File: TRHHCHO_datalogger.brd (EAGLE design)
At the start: 49.1 x 50.8 mm, 39 parts, among them J6 AMP FCI 10103594-0001LF, U1 ATMEGA328P-MU, U10 TSL2591, U2 FT231XQ-R, U3 DS3234, U7 SHT31/35, U8 MCP1703/3.3V, Y2 SPARKFUN_RESONATORSMD

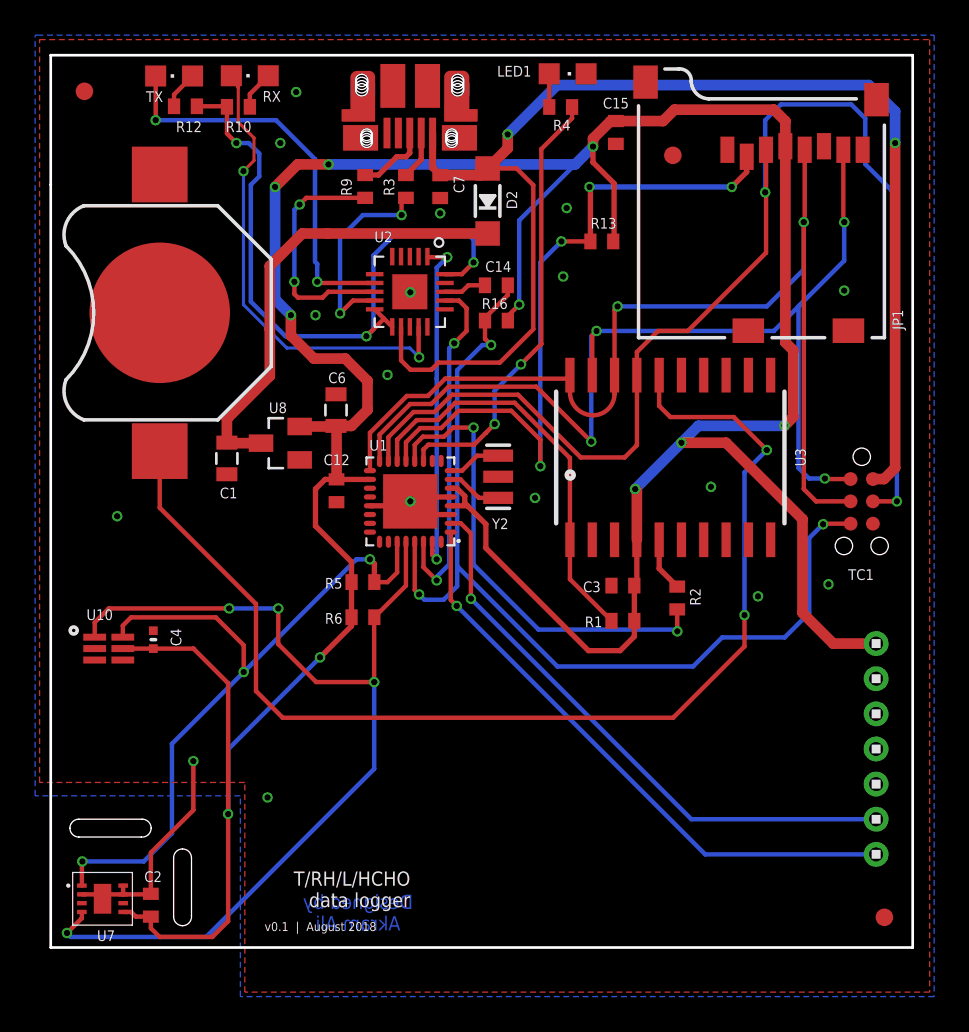
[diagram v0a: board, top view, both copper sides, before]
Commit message: Updated footprint of HCHO sensor
- Now using proper dimensions given by manufacturer
- Small trace adjustments
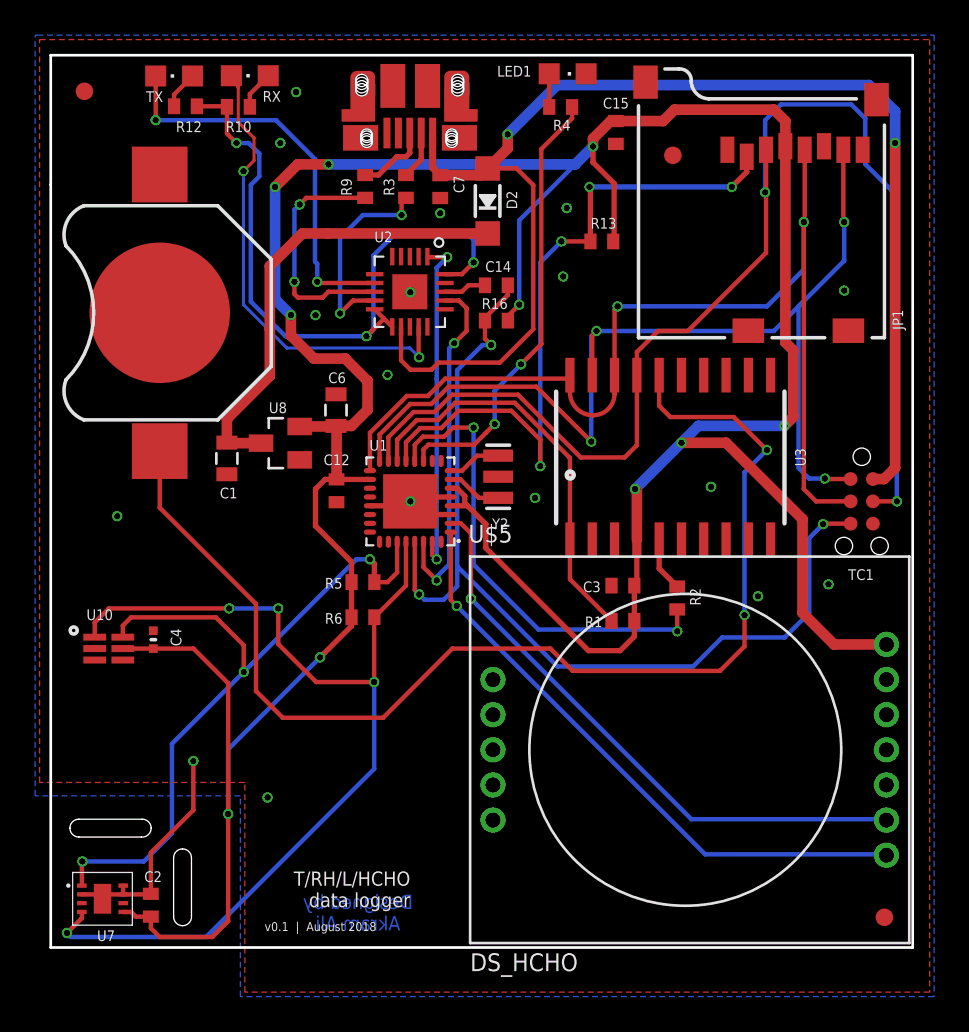
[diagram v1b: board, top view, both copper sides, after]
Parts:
- removed U$4: 1X7, headers(2mm):1X7
- added U$5: DS_HCHO, Plantower-DS-HCHO:DS_HCHO
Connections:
- net D3: now also U$5.P$7; no longer U$4.1
- net D4: now also U$5.P$6; no longer U$4.2
- net GND: now also U$5.P$2; no longer U$4.6
- net VCC: now also U$5.P$1; no longer U$4.7
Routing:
- net N$8: track 66.7 -> 67.7 mm
- net D4: track 33.4 -> 34.0 mm
- net D3: track 34.1 -> 34.7 mm
- net VCC: track 197.5 -> 198.1 mm
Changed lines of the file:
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@@
 <attribute name="NAME" x="33.5382" y="49.5832" size="0.6096" layer="25" font="vector"/>
 </element>
-<element name="U8" library="linear" library_urn="urn:adsk.eagle:library:262" package="SOT23" value="MCP1703/3.3V" x="21.1992" y="28.7124" smashed="yes" rot="R90">
+<element name="U8" library="linear" library_urn="urn:adsk.eagle:library:262" package="SOT23" package3d_urn="urn:adsk.eagle:package:16489/2" value="MCP1703/3.3V" x="21.1992" y="28.7124" smashed="yes" rot="R90">
 <attribute name="MPN" value="MCP1703T-2502E/CB" x="21.1992" y="28.7124" size="1.778" layer="27" rot="R90" display="off"/>
 <attribute name="NAME" x="21.5766" y="31.0322" size="0.6096" layer="25" font="vector" rot="R180"/>
@@
 <attribute name="PROD_ID" value="CONN-13711" x="28.6" y="47.7" size="1.778" layer="27" rot="R180" display="off"/>
 </element>
-<element name="U$4" library="headers(2mm)" package="1X7" value="1X7" x="55.118" y="11.303" rot="R90"/>
 <element name="U10" library="TSL2591" package="DFN6_TAOS" value="TSL2591" x="11.43" y="17.018" smashed="yes">
 <attribute name="MPN" value="TSL25911FN " x="11.43" y="17.018" size="1.778" layer="27" display="off"/>
@@
 <attribute name="NAME" x="14.9543" y="18.161" size="0.6096" layer="25" font="vector" rot="R270"/>
 </element>
+<element name="U$5" library="Plantower-DS-HCHO" package="DS_HCHO" value="DS_HCHO" x="32.004" y="0.254"/>
 </elements>
 <signals>
@@
 <contactref element="TC1" pad="6"/>
 <contactref element="J6" pad="GND"/>
-<contactref element="U$4" pad="6"/>
 <polygon width="0.254" layer="1">
 <vertex x="7.493" y="51.689"/>
@@
 <contactref element="U10" pad="3"/>
 <contactref element="C4" pad="1"/>
+<contactref element="U$5" pad="P$2"/>
 </signal>
 <signal name="VCC">
@@
 <wire x1="23.114" y1="33.528" x2="21.8" y2="34.842" width="0.6096" layer="1"/>
 <wire x1="21.8" y1="34.842" x2="21.8" y2="36" width="0.6096" layer="1"/>
-<contactref element="U$4" pad="7"/>
-<wire x1="55.118" y1="17.303" x2="52.674" y2="17.303" width="0.6096" layer="1"/>
-<wire x1="52.674" y1="17.303" x2="50.927" y2="19.05" width="0.6096" layer="1"/>
 <wire x1="50.927" y1="19.05" x2="50.927" y2="24.384" width="0.6096" layer="1"/>
 <wire x1="46.5755" y1="28.7355" x2="44.0355" y2="28.7355" width="0.6096" layer="1"/>
@@
 <wire x1="25.252" y1="18.308" x2="25.252" y2="18.8032" width="0.3048" layer="1"/>
 <wire x1="16.256" y1="17.018" x2="13.97" y2="17.018" width="0.254" layer="1"/>
+<contactref element="U$5" pad="P$1"/>
+<wire x1="55.704" y1="17.254" x2="52.723" y2="17.254" width="0.6096" layer="1"/>
+<wire x1="52.723" y1="17.254" x2="50.927" y2="19.05" width="0.6096" layer="1"/>
 </signal>
 <signal name="SCL">
@@
 <wire x1="19.812" y1="19.558" x2="19.812" y2="14.605" width="0.254" layer="1"/>
 <wire x1="19.812" y1="14.605" x2="21.336" y2="13.081" width="0.254" layer="1"/>
-<wire x1="43.561" y1="13.081" x2="47.625" y2="17.145" width="0.254" layer="1"/>
 <wire x1="47.625" y1="17.145" x2="47.625" y2="18.923" width="0.254" layer="1"/>
 <via x="47.625" y="18.923" extent="1-16" drill="0.35"/>
 <wire x1="14.3328" y1="25.0372" x2="19.812" y2="19.558" width="0.254" layer="1"/>
-<wire x1="21.336" y1="13.081" x2="43.561" y2="13.081" width="0.254" layer="1"/>
 <wire x1="47.625" y1="27.051" x2="48.895" y2="28.321" width="0.254" layer="16"/>
 <via x="48.895" y="28.321" extent="1-16" drill="0.35"/>
@@
 <wire x1="47.625" y1="18.923" x2="47.625" y2="27.051" width="0.254" layer="16"/>
 <wire x1="47.016" y1="30.2" x2="43.4" y2="30.2" width="0.254" layer="1"/>
+<wire x1="21.336" y1="13.081" x2="27.051" y2="13.081" width="0.254" layer="1"/>
+<wire x1="27.051" y1="13.081" x2="30.988" y2="17.018" width="0.254" layer="1"/>
+<wire x1="30.988" y1="17.018" x2="36.576" y2="17.018" width="0.254" layer="1"/>
+<wire x1="36.576" y1="17.018" x2="37.846" y2="15.748" width="0.254" layer="1"/>
+<wire x1="37.846" y1="15.748" x2="46.228" y2="15.748" width="0.254" layer="1"/>
+<wire x1="46.228" y1="15.748" x2="47.625" y2="17.145" width="0.254" layer="1"/>
 </signal>
 <signal name="SS">
@@
 <signal name="D3">
 <contactref element="U1" pad="1"/>
-<contactref element="U$4" pad="1"/>
 <wire x1="30.9004" y1="23.6488" x2="30.9004" y2="19.7897" width="0.254" layer="1"/>
 <wire x1="30.9004" y1="19.7897" x2="31.242" y2="19.4481" width="0.254" layer="1"/>
 <via x="31.242" y="19.4481" extent="1-16" drill="0.35"/>
 <wire x1="31.242" y1="19.4481" x2="45.3871" y2="5.303" width="0.254" layer="16"/>
-<wire x1="45.3871" y1="5.303" x2="55.118" y2="5.303" width="0.254" layer="16"/>
+<contactref element="U$5" pad="P$7"/>
+<wire x1="45.3871" y1="5.303" x2="55.655" y2="5.303" width="0.254" layer="16"/>
+<wire x1="55.655" y1="5.303" x2="55.704" y2="5.254" width="0.254" layer="16"/>
 </signal>
 <signal name="D4">
 <contactref element="U1" pad="2"/>
-<contactref element="U$4" pad="2"/>
-<wire x1="55.118" y1="7.303" x2="44.6005" y2="7.303" width="0.254" layer="16"/>
-<wire x1="44.6005" y1="7.303" x2="32.04775" y2="19.85575" width="0.254" layer="16"/>
+<wire x1="32.04775" y1="19.85575" x2="44.6005" y2="7.303" width="0.254" layer="16"/>
 <via x="32.04775" y="19.85575" extent="1-16" drill="0.35"/>
 <wire x1="32.04775" y1="23.57825" x2="32.04775" y2="19.85575" width="0.254" layer="1"/>
 <wire x1="30.9004" y1="24.1488" x2="31.4772" y2="24.1488" width="0.254" layer="1"/>
 <wire x1="31.4772" y1="24.1488" x2="32.04775" y2="23.57825" width="0.254" layer="1"/>
+<contactref element="U$5" pad="P$6"/>
+<wire x1="44.6005" y1="7.303" x2="55.655" y2="7.303" width="0.254" layer="16"/>
+<wire x1="55.655" y1="7.303" x2="55.704" y2="7.254" width="0.254" layer="16"/>
 </signal>
 </signals>
@@
 with this version.
 </note>
+<note version="8.3" severity="warning">
+Since Version 8.3, EAGLE supports URNs for individual library
+assets (packages, symbols, and devices). The URNs of those assets
+will not be understood (or retained) with this version.
+</note>
+<note version="8.3" severity="warning">
+Since Version 8.3, EAGLE supports the association of 3D packages
+with devices in libraries, schematics, and board files. Those 3D
+packages will not be understood (or retained) with this version.
+</note>
 </compatibility>

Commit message: minor component placement update
- moved some traces and components so they dont' overlap with silkscreen and keepout
- ERC/DRC
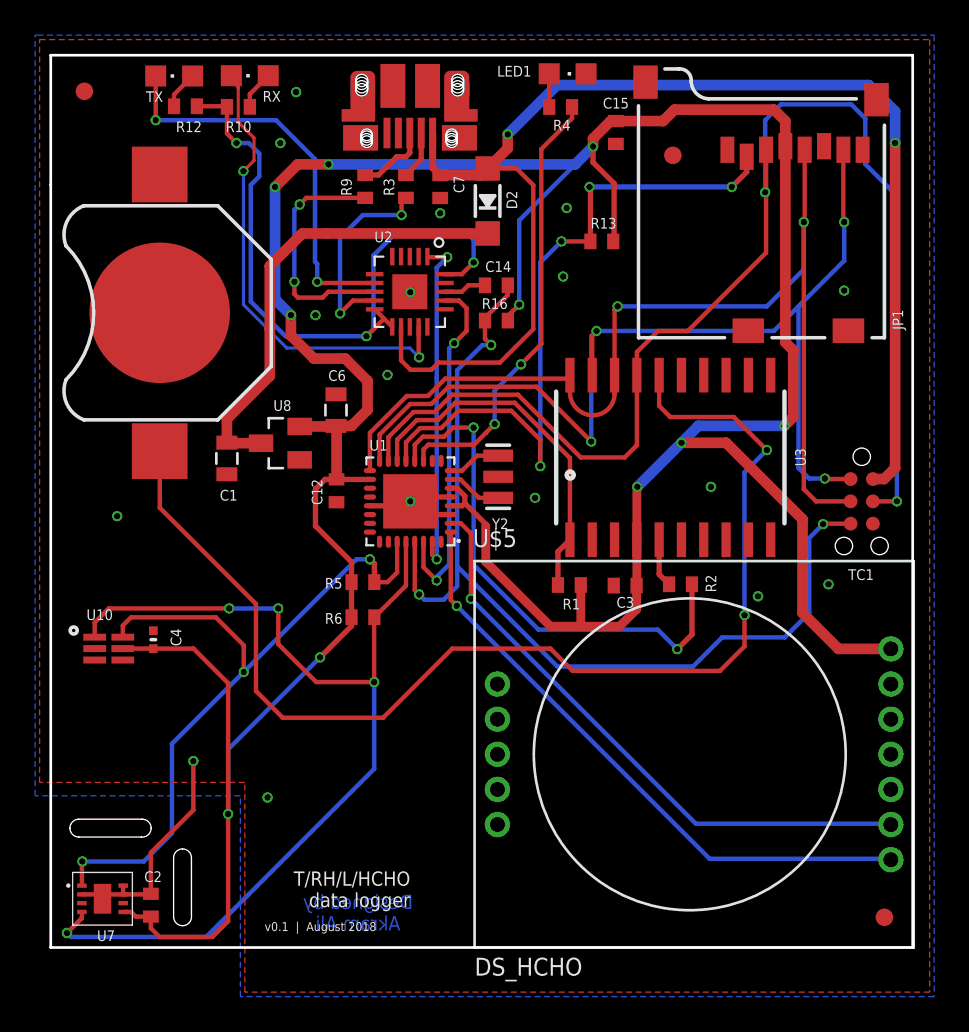
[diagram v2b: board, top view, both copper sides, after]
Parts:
- moved R1 3.66 mm to (37.7, 20.6)
- moved R2 0.80 mm to (44.0, 20.7), turned to 180 degrees
- moved U$5 0.36 mm to (32.3, 0.00)
- moved C3 0.13 mm to (40.8, 20.6)
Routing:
- net D8: track 26.9 -> 30.1 mm
- net SS: track 23.5 -> 20.7 mm
- net VCC: track 198.1 -> 199.2 mm
